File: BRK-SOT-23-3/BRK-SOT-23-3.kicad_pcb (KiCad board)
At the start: 2 copper layers, 18.3 x 22.9 mm, 4 parts, among them J1 Conn_01x03, J2 Conn_01x03, U1 Conn_01x03, U2 Conn_01x03

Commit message: BRK-SOT-23-6, BSK-MSOP-8-3x3-P0.65, BRK-VSSOP-8-2.4x2.1-P0.5
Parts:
- U1, U2: value Conn_01x03 -> SOT-23-3
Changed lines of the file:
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@@
       (effects (font (size 1 1) (thickness 0.15)))
     )
-    (fp_text value Conn_01x03 (at 0 2.5 180) (layer F.Fab) hide
+    (fp_text value SOT-23-3 (at 0 2.5 180) (layer F.Fab) hide
       (effects (font (size 1 1) (thickness 0.15)))
     )
@@
       (effects (font (size 1 1) (thickness 0.15)))
     )
-    (fp_text value Conn_01x03 (at 0 2.5) (layer F.Fab) hide
+    (fp_text value SOT-23-3 (at 0 2.5) (layer F.Fab) hide
       (effects (font (size 1 1) (thickness 0.15)))
     )

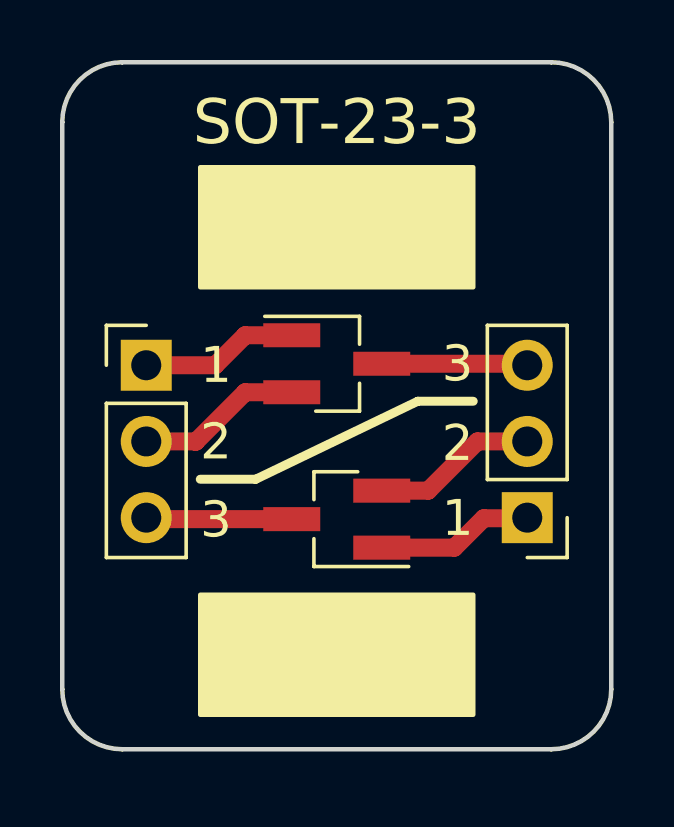
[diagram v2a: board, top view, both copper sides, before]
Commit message: Update several breakout boards
* Reduce distance from edge to pin header
* Enlarge silk screen area
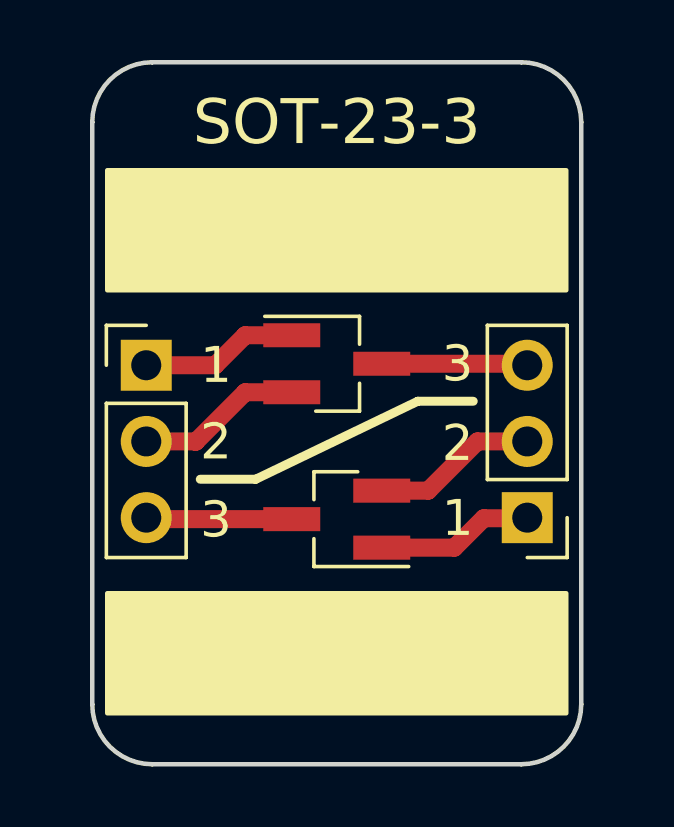
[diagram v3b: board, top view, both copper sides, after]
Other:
- board size 18.3 x 22.9 mm -> 16.3 x 23.4 mm
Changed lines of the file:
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@@
-(kicad_pcb (version 20171130) (host pcbnew 5.0.1-33cea8e~68~ubuntu18.10.1)
+(kicad_pcb (version 20171130) (host pcbnew 5.1.4-e60b266~84~ubuntu19.04.1)
   (general
-    (thickness 1.6)
+    (thickness 1)
     (drawings 20)
     (tracks 18)
@@
   (title_block
     (title BRK-SOT-23-3)
-    (rev v1.0)
+    (rev v1.1)
     (company https://gekkio.fi)
   )
@@
     (zone_45_only no)
     (trace_min 0.2)
-    (segment_width 0.15)
-    (edge_width 0.15)
     (via_size 0.8)
     (via_drill 0.4)
@@
     (uvia_min_size 0.2)
     (uvia_min_drill 0.1)
+    (edge_width 0.15)
+    (segment_width 0.15)
     (pcb_text_width 0.3)
     (pcb_text_size 1.5 1.5)
@@
       (effects (font (size 1 1) (thickness 0.15)))
     )
+    (fp_text user %R (at 0 2.54 90) (layer F.Fab)
+      (effects (font (size 1 1) (thickness 0.15)))
+    )
+    (fp_line (start 1.8 -1.8) (end -1.8 -1.8) (layer F.CrtYd) (width 0.05))
+    (fp_line (start 1.8 6.85) (end 1.8 -1.8) (layer F.CrtYd) (width 0.05))
+    (fp_line (start -1.8 6.85) (end 1.8 6.85) (layer F.CrtYd) (width 0.05))
+    (fp_line (start -1.8 -1.8) (end -1.8 6.85) (layer F.CrtYd) (width 0.05))
+    (fp_line (start -1.33 -1.33) (end 0 -1.33) (layer F.SilkS) (width 0.12))
+    (fp_line (start -1.33 0) (end -1.33 -1.33) (layer F.SilkS) (width 0.12))
+    (fp_line (start -1.33 1.27) (end 1.33 1.27) (layer F.SilkS) (width 0.12))
+    (fp_line (start 1.33 1.27) (end 1.33 6.41) (layer F.SilkS) (width 0.12))
+    (fp_line (start -1.33 1.27) (end -1.33 6.41) (layer F.SilkS) (width 0.12))
+    (fp_line (start -1.33 6.41) (end 1.33 6.41) (layer F.SilkS) (width 0.12))
+    (fp_line (start -1.27 -0.635) (end -0.635 -1.27) (layer F.Fab) (width 0.1))
+    (fp_line (start -1.27 6.35) (end -1.27 -0.635) (layer F.Fab) (width 0.1))
+    (fp_line (start 1.27 6.35) (end -1.27 6.35) (layer F.Fab) (width 0.1))
+    (fp_line (start 1.27 -1.27) (end 1.27 6.35) (layer F.Fab) (width 0.1))
     (fp_line (start -0.635 -1.27) (end 1.27 -1.27) (layer F.Fab) (width 0.1))
-    (fp_line (start 1.27 -1.27) (end 1.27 6.35) (layer F.Fab) (width 0.1))
-    (fp_line (start 1.27 6.35) (end -1.27 6.35) (layer F.Fab) (width 0.1))
-    (fp_line (start -1.27 6.35) (end -1.27 -0.635) (layer F.Fab) (width 0.1))
-    (fp_line (start -1.27 -0.635) (end -0.635 -1.27) (layer F.Fab) (width 0.1))
-    (fp_line (start -1.33 6.41) (end 1.33 6.41) (layer F.SilkS) (width 0.12))
-    (fp_line (start -1.33 1.27) (end -1.33 6.41) (layer F.SilkS) (width 0.12))
-    (fp_line (start 1.33 1.27) (end 1.33 6.41) (layer F.SilkS) (width 0.12))
-    (fp_line (start -1.33 1.27) (end 1.33 1.27) (layer F.SilkS) (width 0.12))
-    (fp_line (start -1.33 0) (end -1.33 -1.33) (layer F.SilkS) (width 0.12))
-    (fp_line (start -1.33 -1.33) (end 0 -1.33) (layer F.SilkS) (width 0.12))
-    (fp_line (start -1.8 -1.8) (end -1.8 6.85) (layer F.CrtYd) (width 0.05))
-    (fp_line (start -1.8 6.85) (end 1.8 6.85) (layer F.CrtYd) (width 0.05))
-    (fp_line (start 1.8 6.85) (end 1.8 -1.8) (layer F.CrtYd) (width 0.05))
-    (fp_line (start 1.8 -1.8) (end -1.8 -1.8) (layer F.CrtYd) (width 0.05))
-    (fp_text user %R (at 0 2.54 90) (layer F.Fab)
-      (effects (font (size 1 1) (thickness 0.15)))
-    )
+    (pad 3 thru_hole oval (at 0 5.08) (size 1.7 1.7) (drill 1) (layers *.Cu *.Mask)
+      (net 4 "Net-(J1-Pad3)"))
+    (pad 2 thru_hole oval (at 0 2.54) (size 1.7 1.7) (drill 1) (layers *.Cu *.Mask)
+      (net 2 "Net-(J1-Pad2)"))
     (pad 1 thru_hole rect (at 0 0) (size 1.7 1.7) (drill 1) (layers *.Cu *.Mask)
       (net 1 "Net-(J1-Pad1)"))
-    (pad 2 thru_hole oval (at 0 2.54) (size 1.7 1.7) (drill 1) (layers *.Cu *.Mask)
-      (net 2 "Net-(J1-Pad2)"))
-    (pad 3 thru_hole oval (at 0 5.08) (size 1.7 1.7) (drill 1) (layers *.Cu *.Mask)
-      (net 4 "Net-(J1-Pad3)"))
     (model ${KISYS3DMOD}/Connector_PinHeader_2.54mm.3dshapes/PinHeader_1x03_P2.54mm_Vertical.wrl
       (at (xyz 0 0 0))
@@
       (effects (font (size 1 1) (thickness 0.15)))
     )
+    (fp_line (start 0.76 1.58) (end -0.7 1.58) (layer F.SilkS) (width 0.12))
+    (fp_line (start -0.7 1.52) (end 0.7 1.52) (layer F.Fab) (width 0.1))
+    (fp_line (start 0.7 -1.52) (end 0.7 1.52) (layer F.Fab) (width 0.1))
+    (fp_line (start -0.7 -0.95) (end -0.15 -1.52) (layer F.Fab) (width 0.1))
+    (fp_line (start -0.15 -1.52) (end 0.7 -1.52) (layer F.Fab) (width 0.1))
+    (fp_line (start -0.7 -0.95) (end -0.7 1.5) (layer F.Fab) (width 0.1))
+    (fp_line (start 0.76 -1.58) (end -2.4 -1.58) (layer F.SilkS) (width 0.12))
+    (fp_line (start -2.7 1.75) (end -2.7 -1.75) (layer F.CrtYd) (width 0.05))
+    (fp_line (start 2.7 1.75) (end -2.7 1.75) (layer F.CrtYd) (width 0.05))
+    (fp_line (start 2.7 -1.75) (end 2.7 1.75) (layer F.CrtYd) (width 0.05))
+    (fp_line (start -2.7 -1.75) (end 2.7 -1.75) (layer F.CrtYd) (width 0.05))
+    (fp_line (start 0.76 -1.58) (end 0.76 -0.65) (layer F.SilkS) (width 0.12))
+    (fp_line (start 0.76 1.58) (end 0.76 0.65) (layer F.SilkS) (width 0.12))
     (fp_text user %R (at 0 0 90) (layer F.Fab)
       (effects (font (size 0.5 0.5) (thickness 0.075)))
     )
-    (fp_line (start 0.76 1.58) (end 0.76 0.65) (layer F.SilkS) (width 0.12))
-    (fp_line (start 0.76 -1.58) (end 0.76 -0.65) (layer F.SilkS) (width 0.12))
-    (fp_line (start -2.7 -1.75) (end 2.7 -1.75) (layer F.CrtYd) (width 0.05))
-    (fp_line (start 2.7 -1.75) (end 2.7 1.75) (layer F.CrtYd) (width 0.05))
-    (fp_line (start 2.7 1.75) (end -2.7 1.75) (layer F.CrtYd) (width 0.05))
-    (fp_line (start -2.7 1.75) (end -2.7 -1.75) (layer F.CrtYd) (width 0.05))
-    (fp_line (start 0.76 -1.58) (end -2.4 -1.58) (layer F.SilkS) (width 0.12))
-    (fp_line (start -0.7 -0.95) (end -0.7 1.5) (layer F.Fab) (width 0.1))
-    (fp_line (start -0.15 -1.52) (end 0.7 -1.52) (layer F.Fab) (width 0.1))
-    (fp_line (start -0.7 -0.95) (end -0.15 -1.52) (layer F.Fab) (width 0.1))
-    (fp_line (start 0.7 -1.52) (end 0.7 1.52) (layer F.Fab) (width 0.1))
-    (fp_line (start -0.7 1.52) (end 0.7 1.52) (layer F.Fab) (width 0.1))
-    (fp_line (start 0.76 1.58) (end -0.7 1.58) (layer F.SilkS) (width 0.12))
+    (pad 3 smd rect (at 1.5 0) (size 1.9 0.8) (layers F.Cu F.Paste F.Mask)
+      (net 3 "Net-(J2-Pad3)"))
+    (pad 2 smd rect (at -1.5 0.95) (size 1.9 0.8) (layers F.Cu F.Paste F.Mask)
+      (net 2 "Net-(J1-Pad2)"))
     (pad 1 smd rect (at -1.5 -0.95) (size 1.9 0.8) (layers F.Cu F.Paste F.Mask)
       (net 1 "Net-(J1-Pad1)"))
-    (pad 2 smd rect (at -1.5 0.95) (size 1.9 0.8) (layers F.Cu F.Paste F.Mask)
-      (net 2 "Net-(J1-Pad2)"))
-    (pad 3 smd rect (at 1.5 0) (size 1.9 0.8) (layers F.Cu F.Paste F.Mask)
-      (net 3 "Net-(J2-Pad3)"))
     (model ${KISYS3DMOD}/Package_TO_SOT_SMD.3dshapes/SOT-23.wrl
       (at (xyz 0 0 0))
@@
     )
   )
-  (gr_arc (start 66.3 70.9) (end 66.3 72.9) (angle -90) (layer Edge.Cuts) (width 0.15))
-  (gr_arc (start 52 70.9) (end 50 70.9) (angle -90) (layer Edge.Cuts) (width 0.15))
-  (gr_arc (start 66.3 52) (end 68.3 52) (angle -90) (layer Edge.Cuts) (width 0.15))
-  (gr_arc (start 52 52) (end 52 50) (angle -90) (layer Edge.Cuts) (width 0.15))
+  (gr_arc (start 65.3 71.4) (end 65.3 73.4) (angle -90) (layer Edge.Cuts) (width 0.15))
+  (gr_arc (start 53 71.4) (end 51 71.4) (angle -90) (layer Edge.Cuts) (width 0.15))
+  (gr_arc (start 65.3 52) (end 67.3 52) (angle -90) (layer Edge.Cuts) (width 0.15))
+  (gr_arc (start 53 52) (end 53 50) (angle -90) (layer Edge.Cuts) (width 0.15))
   (gr_line (start 61.85 61.3) (end 63.7 61.3) (layer F.SilkS) (width 0.3))
   (gr_line (start 56.45 63.9) (end 54.6 63.9) (layer F.SilkS) (width 0.3))
@@
   )
   (gr_line (start 56.45 63.9) (end 61.85 61.3) (layer F.SilkS) (width 0.3))
-  (gr_line (start 66.3 72.9) (end 52 72.9) (layer Edge.Cuts) (width 0.15))
-  (gr_poly (pts (xy 54.6 67.75) (xy 54.6 71.75) (xy 63.7 71.75) (xy 63.7 67.75)) (layer F.SilkS) (width 0.15))
-  (gr_poly (pts (xy 54.6 53.5) (xy 54.6 57.5) (xy 63.7 57.5) (xy 63.7 53.5)) (layer F.SilkS) (width 0.15))
-  (gr_line (start 68.3 52) (end 68.3 70.9) (layer Edge.Cuts) (width 0.15))
+  (gr_line (start 65.3 73.4) (end 53 73.4) (layer Edge.Cuts) (width 0.15))
+  (gr_poly (pts (xy 51.5 67.7) (xy 51.5 71.7) (xy 66.8 71.7) (xy 66.8 67.7)) (layer F.SilkS) (width 0.15))
+  (gr_poly (pts (xy 51.5 53.6) (xy 51.5 57.6) (xy 66.8 57.6) (xy 66.8 53.6)) (layer F.SilkS) (width 0.15))
+  (gr_line (start 67.3 52) (end 67.3 71.4) (layer Edge.Cuts) (width 0.15))
   (gr_text SOT-23-3 (at 59.15 52) (layer F.SilkS)
     (effects (font (size 1.5 1.5) (thickness 0.3)))
   )
-  (gr_line (start 52 50) (end 66.3 50) (layer Edge.Cuts) (width 0.15))
-  (gr_line (start 50 70.9) (end 50 52) (layer Edge.Cuts) (width 0.15))
+  (gr_line (start 53 50) (end 65.3 50) (layer Edge.Cuts) (width 0.15))
+  (gr_line (start 51 71.4) (end 51 52) (layer Edge.Cuts) (width 0.15))
   (segment (start 56.1 59.1) (end 55.1 60.1) (width 0.6) (layer F.Cu) (net 1))
   (segment (start 57.65 59.1) (end 56.1 59.1) (width 0.6) (layer F.Cu) (net 1))
